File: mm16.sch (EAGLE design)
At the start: 93 parts, among them IC101 ATMEGA32-PU, IC102 DS1337, IC103 MAX483CPA, IC104 74HC594N, IC105 74HC594N, IC201 LTV847, IC202 LTV847, IC203 LTV847, IC204 LTV847, K301 S202S02, K302 S202S02, K303 S202S02, K304 S202S02, K305 S202S02, K306 S202S02, K307 S202S02, K308 S202S02, K309 S202S02, K310 S202S02, K311 S202S02, K312 S202S02, K313 S202S02, K314 S202S02, K315 S202S02, K316 S202S02, Q1 32,768kHz

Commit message: Multimaster mit 16 Eingängen erstellt
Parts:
- removed C104, C105: 10nF, passiv:C_025-025X050
- removed IC104, IC105: 74HC594N, 74xx-eu:74HC594N
- removed K301, K302, K303, K304, K305, K306, K307, K308, K309, K310, K311, K312, K313, K314, K315, K316: S202S02, relais:S202S02
- removed R301, R302, R303, R304, R305, R306, R307, R308, R309, R310, R311, R312, R313, R314, R315, R316: (no value), passiv:R_0204/2V
- removed X101: (no value), anschlussklemmen:233-504
- removed X201, X202, X203, X204, X301, X302, X303, X304: (no value), anschlussklemmen:233-508
- added X1: (no value), anschluss:WS16V
- added X2, X3: (no value), anschluss:WAGO_236-408
- added X4, X5, X6: (no value), anschluss:WAGO_236-402
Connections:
- removed net N$100: K306.DS1, X302-3.-1
- removed net N$101: K306.DS2, X302-4.-1
- removed net N$102: K307.DS1, X302-5.-1
- removed net N$103: K307.DS2, X302-6.-1
- removed net N$104: K308.DS1, X302-7.-1
- removed net N$105: K308.DS2, X302-8.-1
- removed net N$106: K309.DS1, X303-1.-1
- removed net N$107: K309.DS2, X303-2.-1
- removed net N$108: K310.DS1, X303-3.-1
- removed net N$109: K310.DS2, X303-4.-1
- removed net N$110: K311.DS1, X303-5.-1
- removed net N$111: K311.DS2, X303-6.-1
- removed net N$112: K312.DS1, X303-7.-1
- removed net N$113: K312.DS2, X303-8.-1
- removed net N$114: K313.DS1, X304-1.-1
- removed net N$115: K313.DS2, X304-2.-1
- removed net N$116: K314.DS1, X304-3.-1
- removed net N$117: K314.DS2, X304-4.-1
- removed net N$118: K315.DS1, X304-5.-1
- removed net N$119: K315.DS2, X304-6.-1
- removed net N$120: K316.DS1, X304-7.-1
- removed net N$121: K316.DS2, X304-8.-1
- removed net N$124: IC103G$1.B, X101-4.-1
- removed net N$21: K305.A, R305.2
- removed net N$22: K306.A, R306.2
- removed net N$23: K307.A, R307.2
- removed net N$24: K308.A, R308.2
- removed net N$41: K309.A, R309.2
- removed net N$43: K310.A, R310.2
- removed net N$44: K311.A, R311.2
- removed net N$45: K312.A, R312.2
- removed net N$46: K313.A, R313.2
- removed net N$47: K314.A, R314.2
- removed net N$48: K315.A, R315.2
- removed net N$49: K316.A, R316.2
- removed net N$51: R204.1, X201-2.-1
- removed net N$53: R203.1, X201-4.-1
- removed net N$54: R202.1, X201-6.-1
- removed net N$56: R201.1, X201-8.-1
- removed net N$58: IC104A.QH*, IC105A.SER
- removed net N$59: V101.-VIN, X101-1.-1
- removed net N$60: V101.+VIN, X101-2.-1
- removed net N$66: R205.1, X202-8.-1
- removed net N$68: R206.1, X202-6.-1
- removed net N$70: R207.1, X202-4.-1
- removed net N$72: R208.1, X202-2.-1
- removed net N$74: IC103G$1.A, X101-3.-1
- removed net N$75: R216.1, X204-2.-1
- removed net N$76: R215.1, X204-4.-1
- removed net N$78: R214.1, X204-6.-1
- removed net N$80: R213.1, X204-8.-1
- removed net N$82: R212.1, X203-2.-1
- removed net N$84: R211.1, X203-4.-1
- removed net N$87: R209.1, X203-8.-1
- removed net N$89: R210.1, X203-6.-1
- removed net N$90: K301.DS1, X301-1.-1
- removed net N$91: K301.DS2, X301-2.-1
- removed net N$92: K302.DS1, X301-3.-1
- removed net N$93: K302.DS2, X301-4.-1
- removed net N$94: K303.DS1, X301-5.-1
- removed net N$95: K303.DS2, X301-6.-1
- removed net N$96: K304.DS1, X301-7.-1
- removed net N$97: K304.DS2, X301-8.-1
- removed net N$98: K305.DS1, X302-1.-1
- removed net N$99: K305.DS2, X302-2.-1
- removed net OUT0: IC104A.QA, R301.1
- removed net OUT1: IC104A.QB, R302.1
- removed net OUT10: IC105A.QC, R311.1
- removed net OUT11: IC105A.QD, R312.1
- removed net OUT12: IC105A.QE, R313.1
- removed net OUT13: IC105A.QF, R314.1
- removed net OUT14: IC105A.QG, R315.1
- removed net OUT15: IC105A.QH, R316.1
- removed net OUT2: IC104A.QC, R303.1
- removed net OUT3: IC104A.QD, R304.1
- removed net OUT4: IC104A.QE, R305.1
- removed net OUT5: IC104A.QF, R306.1
- removed net OUT6: IC104A.QG, R307.1
- removed net OUT7: IC104A.QH, R308.1
- removed net OUT8: IC105A.QA, R309.1
- removed net OUT9: IC105A.QB, R310.1
- new net GNDIO: R201.1, R202.1, R203.1, R204.1, R205.1, R206.1, R207.1, R208.1, R209.1, R210.1, R211.1, R212.1, R213.1, R214.1, R215.1, R216.1, X4.1.A, X4.1.B, X4.2.A, X4.2.B
- net !R: now also X1-10.A, X1-9.A; no longer IC104A.RCL, IC104A.SCL, IC105A.RCL, IC105A.SCL
- net +5V: now also X1-1.A, X1-2.A, X1-3.A, X1-4.A; no longer C104.1, C105.1, IC104P.VCC, IC105P.VCC
- net C1: now also X1-5.A, X1-6.A; no longer IC104A.SCK, IC105A.SCK
- net C2: now also X1-7.A, X1-8.A; no longer IC104A.RCK, IC105A.RCK
- net D: now also X1-11.A, X1-12.A; no longer IC104A.SER
- net GND: now also X1-13.A, X1-14.A, X1-15.A, X1-16.A; no longer C104.2, C105.2, IC104P.GND, IC105P.GND, K301.K, K302.K, K303.K, K304.K, K305.K, K306.K, K307.K, K308.K, K309.K, K310.K, K311.K, K312.K, K313.K, K314.K, K315.K, K316.K
- net N$17: now also V101.+VIN, X5.1.A, X5.1.B; no longer K301.A, R301.2
- net N$18: now also V101.-VIN, X5.2.A, X5.2.B; no longer K302.A, R302.2
- net N$19: now also IC103G$1.B, X6.2.A, X6.2.B; no longer K303.A, R303.2
- net N$20: now also IC103G$1.A, X6.1.A, X6.1.B; no longer K304.A, R304.2
- net N$50: now also X2.5.A, X2.5.B; no longer X201-1.-1
- net N$52: now also X2.6.A, X2.6.B; no longer X201-3.-1
- net N$55: now also X2.7.A, X2.7.B; no longer X201-5.-1
- net N$57: now also X2.8.A, X2.8.B; no longer X201-7.-1
- net N$65: now also X2.4.A, X2.4.B; no longer X202-7.-1
- net N$67: now also X2.3.A, X2.3.B; no longer X202-5.-1
- net N$69: now also X2.2.A, X2.2.B; no longer X202-3.-1
- net N$71: now also X2.1.A, X2.1.B; no longer X202-1.-1
- net N$73: now also X3.1.A, X3.1.B; no longer X204-1.-1
- net N$77: now also X3.2.A, X3.2.B; no longer X204-3.-1
- net N$79: now also X3.3.A, X3.3.B; no longer X204-5.-1
- net N$81: now also X3.4.A, X3.4.B; no longer X204-7.-1
- net N$83: now also X3.5.A, X3.5.B; no longer X203-1.-1
- net N$85: now also X3.6.A, X3.6.B; no longer X203-3.-1
- net N$86: now also X3.8.A, X3.8.B; no longer X203-7.-1
- net N$88: now also X3.7.A, X3.7.B; no longer X203-5.-1

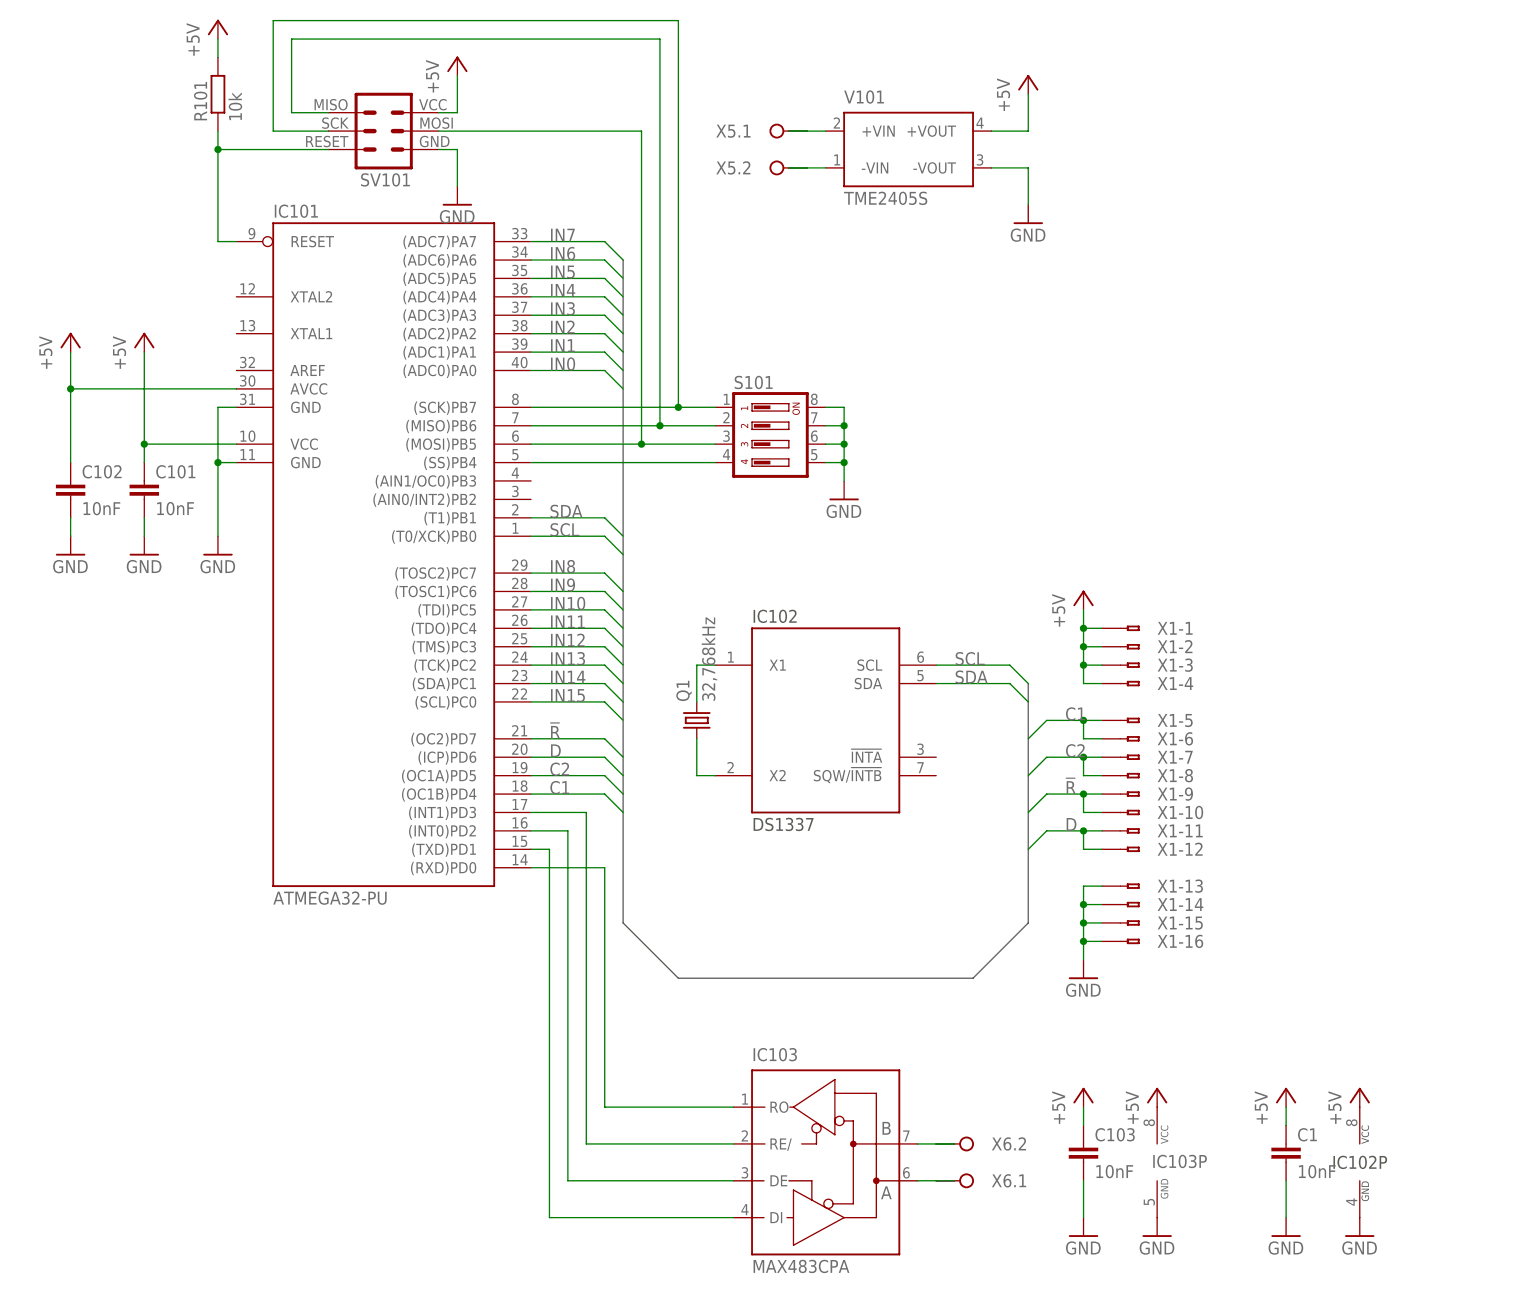
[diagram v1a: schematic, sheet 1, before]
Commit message: Batterie auf Multimaster hinzugefügt
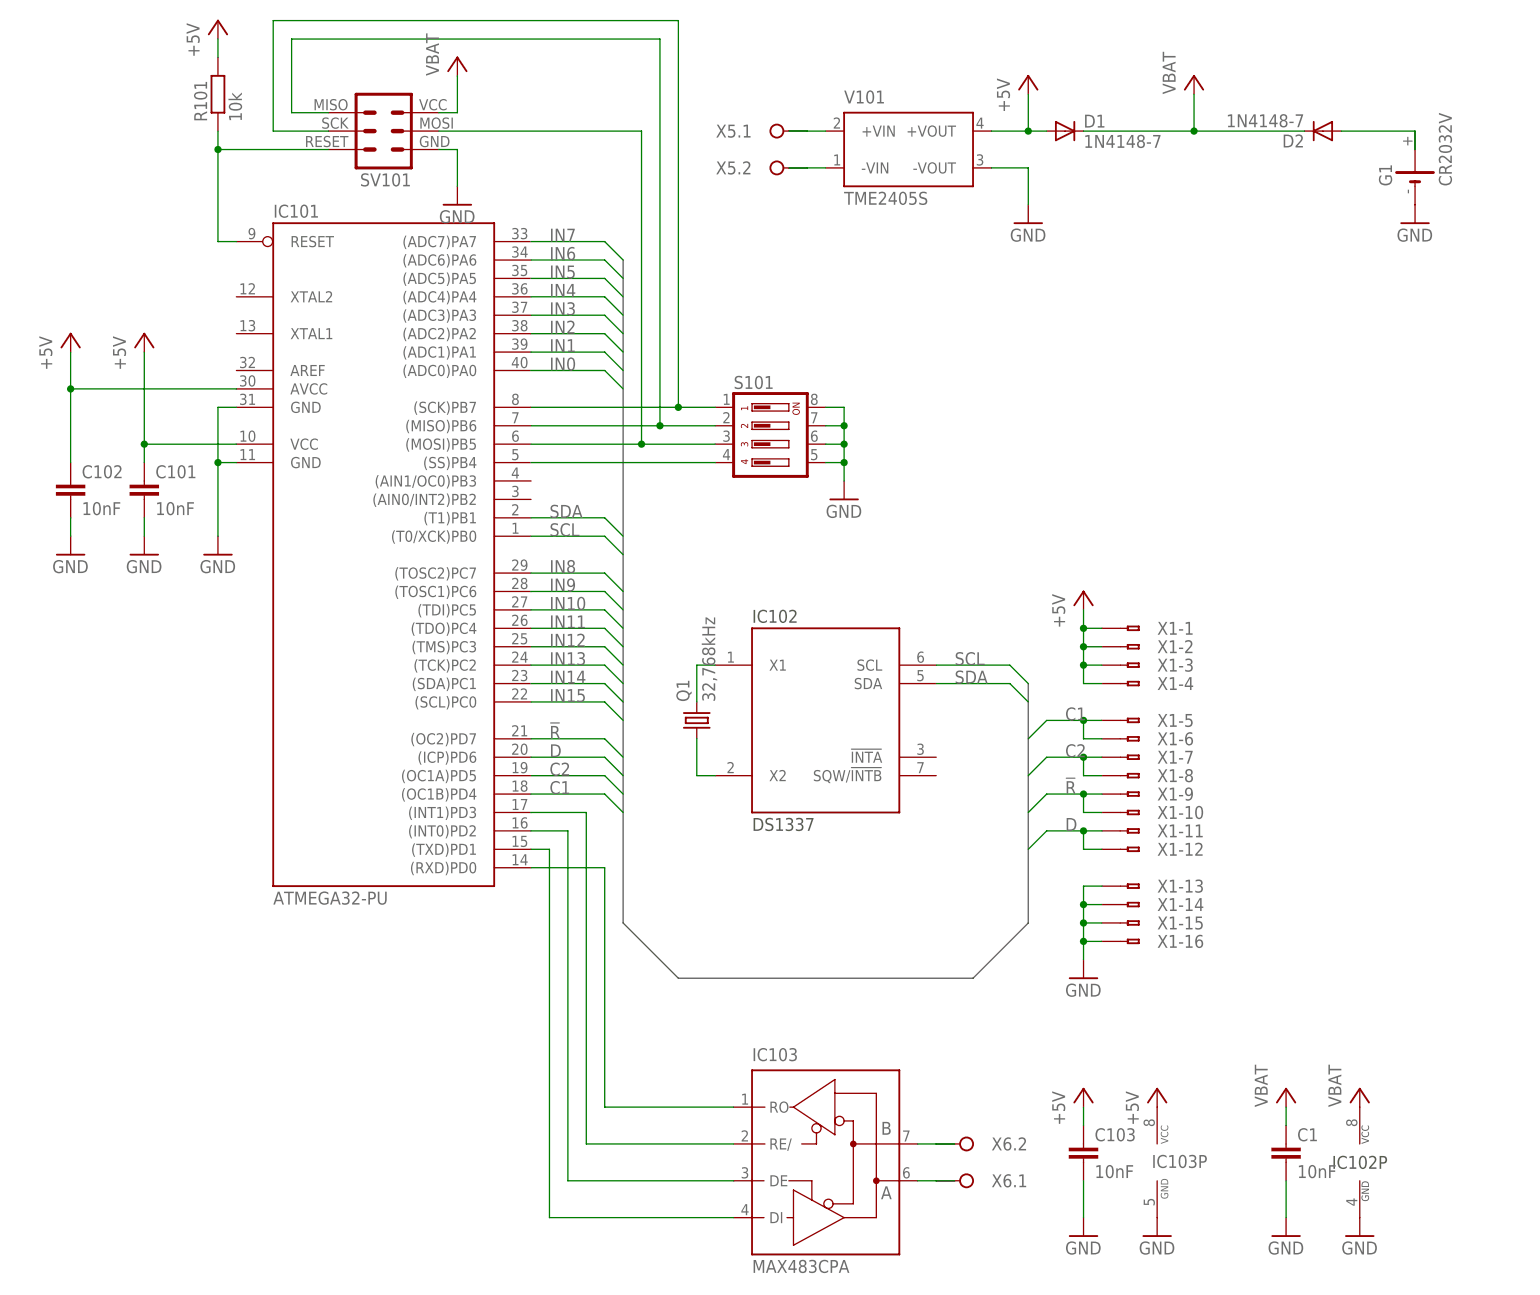
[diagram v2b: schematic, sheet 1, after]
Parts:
- added D1, D2: 1N4148-7, diode:1N4148-7
- added G1: CR2032V, battery:CR2032V
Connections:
- new net N$21: D2.A, G1.+, G1.+@1
- new net VCC: C1.1, D1.C, D2.C, IC102P.VCC, SV101.VCC
- net +5V: now also D1.A; no longer C1.1, IC102P.VCC, SV101.VCC
- net GND: now also G1.-
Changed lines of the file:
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@@
 <part name="SV101" library="stecker" deviceset="AVR_ISP6" device=""/>
 <part name="GND25" library="versorgung" deviceset="GND" device=""/>
-<part name="P+2" library="versorgung" deviceset="+5V" device=""/>
 <part name="R101" library="passiv" deviceset="R_" device="0204/2V" value="10k"/>
 <part name="P+1" library="versorgung" deviceset="+5V" device=""/>
@@
 <part name="Q1" library="passiv" deviceset="Q_" device="HC49S" value="32,768kHz"/>
 <part name="C1" library="passiv" deviceset="C_" device="025-025X050" value="10nF"/>
-<part name="P+12" library="versorgung" deviceset="+5V" device=""/>
-<part name="P+13" library="versorgung" deviceset="+5V" device=""/>
 <part name="GND45" library="versorgung" deviceset="GND" device=""/>
 <part name="GND46" library="versorgung" deviceset="GND" device=""/>
@@
 <part name="X6" library="anschluss" deviceset="WAGO_236-402" device=""/>
 <part name="X1" library="anschluss" deviceset="WS16" device="V"/>
+<part name="P+7" library="versorgung" deviceset="VCC" device="" value="VBAT"/>
+<part name="P+2" library="versorgung" deviceset="VCC" device="" value="VBAT"/>
+<part name="P+8" library="versorgung" deviceset="VCC" device="" value="VBAT"/>
+<part name="P+9" library="versorgung" deviceset="VCC" device="" value="VBAT"/>
+<part name="D1" library="diode" deviceset="1N4148" device="-7"/>
+<part name="D2" library="diode" deviceset="1N4148" device="-7"/>
+<part name="G1" library="battery" deviceset="CR2032V" device=""/>
+<part name="GND39" library="versorgung" deviceset="GND" device=""/>
 </parts>
 <sheets>
@@
 <instance part="SV101" gate="1" x="76.2" y="157.48" rot="R180"/>
 <instance part="GND25" gate="1" x="86.36" y="147.32"/>
-<instance part="P+2" gate="1" x="86.36" y="167.64"/>
 <instance part="R101" gate="G$1" x="53.34" y="162.56" rot="R90"/>
 <instance part="P+1" gate="1" x="53.34" y="172.72"/>
@@
 <instance part="IC102" gate="P" x="210.82" y="15.24"/>
 <instance part="C1" gate="G$1" x="200.66" y="17.78"/>
-<instance part="P+12" gate="1" x="200.66" y="25.4"/>
-<instance part="P+13" gate="1" x="210.82" y="25.4"/>
 <instance part="GND45" gate="1" x="200.66" y="5.08"/>
 <instance part="GND46" gate="1" x="210.82" y="5.08"/>
@@
 <instance part="X1" gate="-15" x="180.34" y="48.26" rot="R180"/>
 <instance part="X1" gate="-16" x="180.34" y="45.72" rot="R180"/>
+<instance part="P+7" gate="VCC" x="187.96" y="165.1"/>
+<instance part="P+2" gate="VCC" x="86.36" y="167.64"/>
+<instance part="P+8" gate="VCC" x="210.82" y="25.4"/>
+<instance part="P+9" gate="VCC" x="200.66" y="25.4"/>
+<instance part="D1" gate="G$1" x="170.18" y="157.48"/>
+<instance part="D2" gate="G$1" x="205.74" y="157.48" rot="R180"/>
+<instance part="G1" gate="1" x="218.44" y="152.4" rot="R90"/>
+<instance part="GND39" gate="1" x="218.44" y="144.78"/>
 </instances>
 <busses>
@@
 <pinref part="X1" gate="-16" pin="A"/>
 </segment>
+<segment>
+<pinref part="G1" gate="1" pin="-"/>
+<pinref part="GND39" gate="1" pin="GND"/>
+</segment>
 </net>
 <net name="IN0" class="0">
@@
 <net name="+5V" class="0">
 <segment>
-<pinref part="P+2" gate="1" pin="+5V"/>
-<pinref part="SV101" gate="1" pin="VCC"/>
-<wire x1="86.36" y1="165.1" x2="86.36" y2="160.02" width="0.1524" layer="91"/>
-<wire x1="86.36" y1="160.02" x2="83.82" y2="160.02" width="0.1524" layer="91"/>
-</segment>
-<segment>
 <pinref part="R101" gate="G$1" pin="2"/>
 <pinref part="P+1" gate="1" pin="+5V"/>
@@
 <pinref part="V101" gate="G$1" pin="+VOUT"/>
 <wire x1="165.1" y1="157.48" x2="160.02" y2="157.48" width="0.1524" layer="91"/>
+<pinref part="D1" gate="G$1" pin="A"/>
+<wire x1="165.1" y1="157.48" x2="167.64" y2="157.48" width="0.1524" layer="91"/>
+<junction x="165.1" y="157.48"/>
 </segment>
 <segment>
@@
 <pinref part="P+11" gate="1" pin="+5V"/>
 <pinref part="IC103" gate="P" pin="VCC"/>
-</segment>
-<segment>
-<pinref part="IC102" gate="P" pin="VCC"/>
-<pinref part="P+13" gate="1" pin="+5V"/>
-</segment>
-<segment>
-<pinref part="P+12" gate="1" pin="+5V"/>
-<pinref part="C1" gate="G$1" pin="1"/>
-<wire x1="200.66" y1="22.86" x2="200.66" y2="20.32" width="0.1524" layer="91"/>
 </segment>
 <segment>
@@
 </segment>
 </net>
+<net name="VCC" class="0">
+<segment>
+<pinref part="SV101" gate="1" pin="VCC"/>
+<wire x1="86.36" y1="165.1" x2="86.36" y2="160.02" width="0.1524" layer="91"/>
+<wire x1="86.36" y1="160.02" x2="83.82" y2="160.02" width="0.1524" layer="91"/>
+<pinref part="P+2" gate="VCC" pin="VCC"/>
+</segment>
+<segment>
+<pinref part="IC102" gate="P" pin="VCC"/>
+<pinref part="P+8" gate="VCC" pin="VCC"/>
+</segment>
+<segment>
+<pinref part="C1" gate="G$1" pin="1"/>
+<wire x1="200.66" y1="22.86" x2="200.66" y2="20.32" width="0.1524" layer="91"/>
+<pinref part="P+9" gate="VCC" pin="VCC"/>
+</segment>
+<segment>
+<pinref part="D1" gate="G$1" pin="C"/>
+<pinref part="P+7" gate="VCC" pin="VCC"/>
+<wire x1="172.72" y1="157.48" x2="187.96" y2="157.48" width="0.1524" layer="91"/>
+<wire x1="187.96" y1="157.48" x2="187.96" y2="162.56" width="0.1524" layer="91"/>
+<pinref part="D2" gate="G$1" pin="C"/>
+<wire x1="203.2" y1="157.48" x2="187.96" y2="157.48" width="0.1524" layer="91"/>
+<junction x="187.96" y="157.48"/>
+</segment>
+</net>
+<net name="N$21" class="0">
+<segment>
+<pinref part="D2" gate="G$1" pin="A"/>
+<pinref part="G1" gate="1" pin="+"/>
+<wire x1="208.28" y1="157.48" x2="218.44" y2="157.48" width="0.1524" layer="91"/>
+<pinref part="G1" gate="1" pin="+@1"/>
+<wire x1="218.44" y1="157.48" x2="218.44" y2="154.94" width="0.1524" layer="91"/>
+</segment>
+</net>
